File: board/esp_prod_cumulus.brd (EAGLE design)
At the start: 22 parts, among them K3 ZF112, X1 332-02, X7 332-02, X8 332-02, X9 332-02

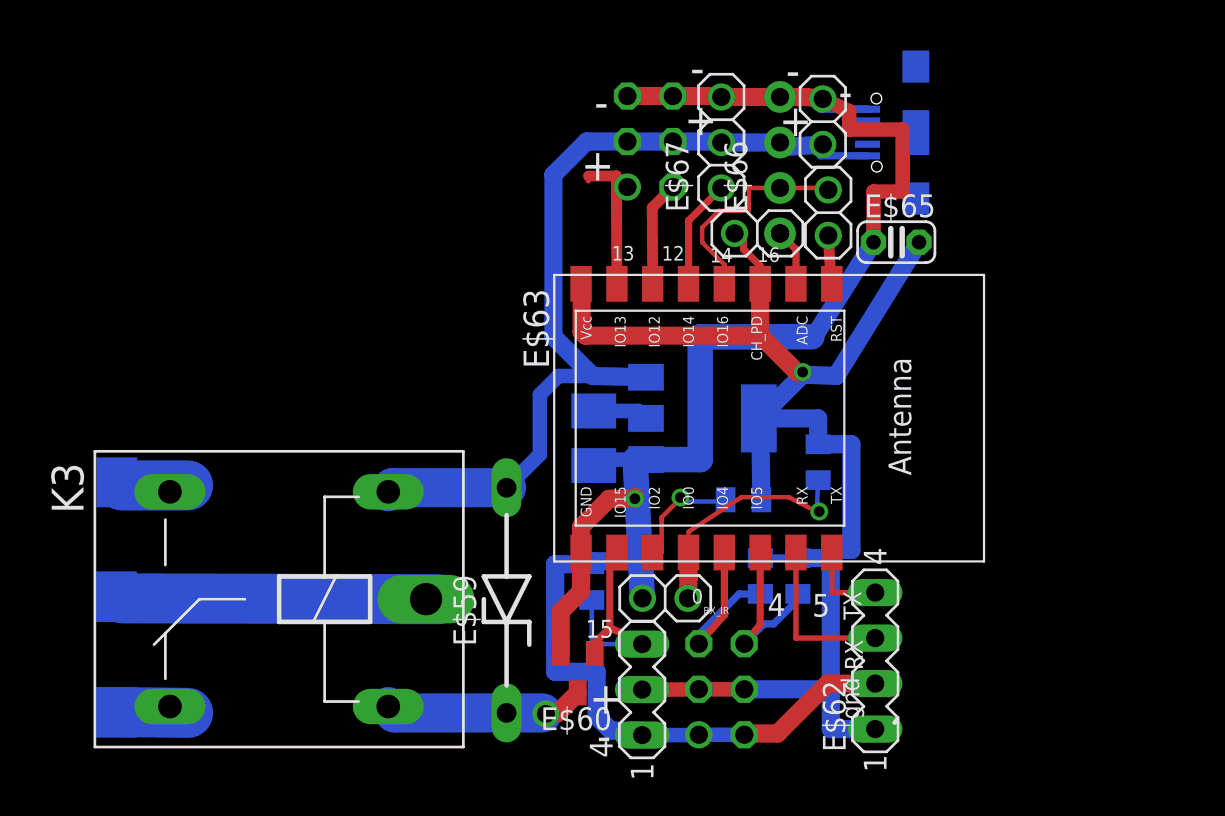
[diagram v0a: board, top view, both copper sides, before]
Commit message: Modification layout + ajout instructions fichier README.md
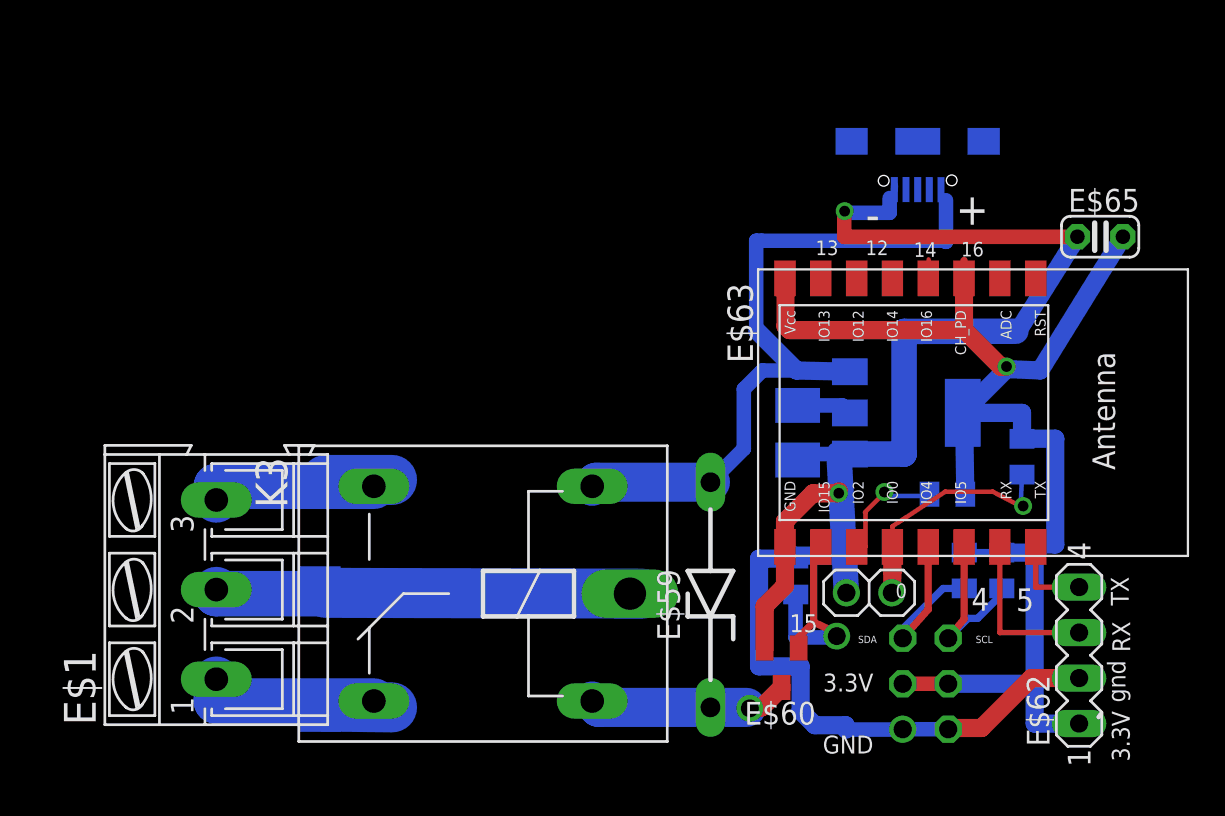
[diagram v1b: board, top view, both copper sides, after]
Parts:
- removed 4: (no value), con-lstb:MA03-1
- removed E$61: (no value), con-lstb:MA03-2
- removed E$66: (no value), adafruit:1X04-CLEANBIG
- removed E$67: (no value), adafruit:1X03
- removed X1, X7, X9: 332-02, aaaa:1X02
- added E$1: (no value), con-ptr500:AK300/3
- moved E$71 11.4 mm to (49.6, 12.3)
- moved E$49 11.4 mm to (44.3, 21.1)
- moved E$59 11.4 mm to (33.4, 11.0)
- moved E$60 11.4 mm to (37.3, 6.89)
- moved E$62 11.4 mm to (53.9, 7.58)
- moved E$63 11.4 mm to (47.0, 21.1)
- moved E$64 11.4 mm to (45.4, 6.00)
- moved E$65 11.4 mm to (55.1, 31.0)
- moved E$68 11.4 mm to (46.6, 16.6)
- moved E$69 11.4 mm to (50.8, 18.7)
- moved E$70 11.4 mm to (38.1, 12.0)
- moved E$72 11.4 mm to (47.5, 12.3)
- moved K3 11.4 mm to (20.7, 11.0)
- moved X8 11.4 mm to (41.0, 11.1)
- moved E$73 11.4 mm to (38.2, 20.0)
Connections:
- removed net S$108: E$63.4, E$66.2, X7.2
- removed net S$110: E$61.1, E$63.7
- removed net S$111: E$61.2, E$63.6
- removed net S$126: E$63.5, E$67.1
- removed net S$127: E$63.2, E$66.1
- new net S$10: E$63.4
- new net S$6: E$1.3, K3.S
- new net S$7: E$1.2, K3.P
- new net S$8: E$1.1, K3.O
- new net S$9: E$60.1, E$63.10
- net S$104: no longer 4.3, E$60.1, E$63.10
- net S$109: no longer E$61.3, E$61.4, E$66.3, E$67.2, X1.1
- net S$112: no longer X7.1
- net S$131: no longer 4.2, X9.2
- net S$83: no longer 4.1, E$61.5, E$61.6, E$66.4, E$67.3, X1.2
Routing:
- net S$109: track 50.4 -> 22.1 mm
- net S$83: track 106.1 -> 78.1 mm
- net S$7: track 0.00 -> 23.3 mm
- net S$14: track 0.00 -> 14.4 mm
- net S$108: track 12.7 -> 0.00 mm
- net S$11: track 0.00 -> 10.2 mm
- net S$8: track 0.00 -> 10.0 mm
- net S$6: track 0.00 -> 9.56 mm
- net S$110: track 8.72 -> 0.00 mm
- net S$104: track 13.5 -> 5.28 mm
- net S$9: track 0.00 -> 7.34 mm
- net S$126: track 6.11 -> 0.00 mm
- net S$111: track 5.88 -> 0.00 mm
- net S$131: track 81.9 -> 76.0 mm
- net S$13: track 0.00 -> 5.32 mm
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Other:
- board text added: "3.3V"
- board text added: "GND"
- board text added: "SCL"
- board text added: "SDA"
- board text removed: "RX_IR"
